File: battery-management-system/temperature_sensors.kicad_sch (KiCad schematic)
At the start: 4 parts, among them J15 TEMP_CELL1, J16 TEMP_CELL2, J17 TEMP_CELL3, J18 TEMP_CELL4

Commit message: improve layout
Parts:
- renumbered J15 to J22, J16 to J23, J17 to J24, J18 to J25
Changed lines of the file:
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@@
   (symbol (lib_id "benediktibk:rspro_header_4pin_3_5mm") (at 58.42 53.34 0) (unit 1)
     (in_bom yes) (on_board yes) (dnp no)
-    (property "Reference" "J17" (at 60.96 53.34 0)
+    (property "Reference" "J24" (at 60.96 53.34 0)
       (effects (font (size 1.27 1.27)) (justify left))
     )
@@
       (project "battery-management-system"
         (path "/5272f0ff-3069-41a9-bca2-80beede8b4b2/3cb0d78b-1dc8-4b57-8c9a-18900dc8da61"
-          (reference "J17") (unit 1)
+          (reference "J24") (unit 1)
         )
       )
@@
   (symbol (lib_id "benediktibk:rspro_header_4pin_3_5mm") (at 58.42 27.94 0) (unit 1)
     (in_bom yes) (on_board yes) (dnp no)
-    (property "Reference" "J15" (at 60.96 27.94 0)
+    (property "Reference" "J22" (at 60.96 27.94 0)
       (effects (font (size 1.27 1.27)) (justify left))
     )
@@
       (project "battery-management-system"
         (path "/5272f0ff-3069-41a9-bca2-80beede8b4b2/3cb0d78b-1dc8-4b57-8c9a-18900dc8da61"
-          (reference "J15") (unit 1)
+          (reference "J22") (unit 1)
         )
       )
@@
   (symbol (lib_id "benediktibk:rspro_header_4pin_3_5mm") (at 58.42 40.64 0) (unit 1)
     (in_bom yes) (on_board yes) (dnp no)
-    (property "Reference" "J16" (at 60.96 40.64 0)
+    (property "Reference" "J23" (at 60.96 40.64 0)
       (effects (font (size 1.27 1.27)) (justify left))
     )
@@
       (project "battery-management-system"
         (path "/5272f0ff-3069-41a9-bca2-80beede8b4b2/3cb0d78b-1dc8-4b57-8c9a-18900dc8da61"
-          (reference "J16") (unit 1)
+          (reference "J23") (unit 1)
         )
       )
@@
   (symbol (lib_id "power:GND") (at 49.53 74.93 0) (unit 1)
     (in_bom yes) (on_board yes) (dnp no) (fields_autoplaced)
-    (property "Reference" "#PWR09" (at 49.53 81.28 0)
+    (property "Reference" "#PWR082" (at 49.53 81.28 0)
       (effects (font (size 1.27 1.27)) hide)
     )
@@
       (project "battery-management-system"
         (path "/5272f0ff-3069-41a9-bca2-80beede8b4b2/3cb0d78b-1dc8-4b57-8c9a-18900dc8da61"
-          (reference "#PWR09") (unit 1)
+          (reference "#PWR082") (unit 1)
         )
       )
@@
   (symbol (lib_id "benediktibk:rspro_header_4pin_3_5mm") (at 58.42 66.04 0) (unit 1)
     (in_bom yes) (on_board yes) (dnp no)
-    (property "Reference" "J18" (at 60.96 66.04 0)
+    (property "Reference" "J25" (at 60.96 66.04 0)
       (effects (font (size 1.27 1.27)) (justify left))
     )
@@
       (project "battery-management-system"
         (path "/5272f0ff-3069-41a9-bca2-80beede8b4b2/3cb0d78b-1dc8-4b57-8c9a-18900dc8da61"
-          (reference "J18") (unit 1)
+          (reference "J25") (unit 1)
         )
       )

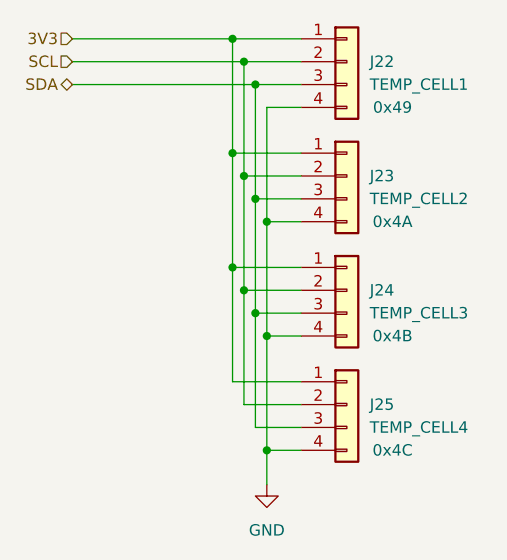
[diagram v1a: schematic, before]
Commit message: add enable input for cell measurement
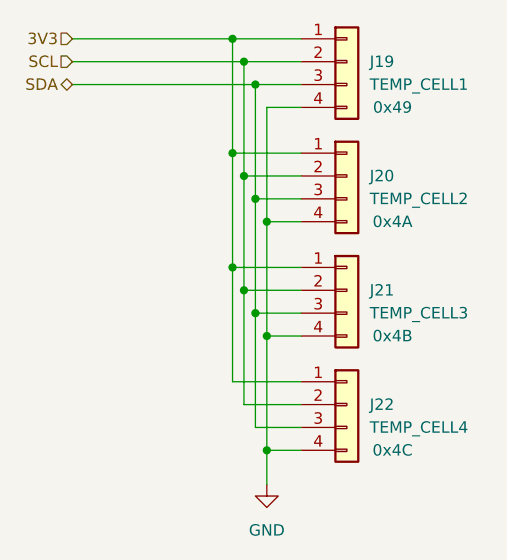
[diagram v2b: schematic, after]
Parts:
- renumbered J22 to J19, J23 to J20, J24 to J21, J25 to J22
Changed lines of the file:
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@@
   (symbol (lib_id "benediktibk:rspro_header_4pin_3_5mm") (at 58.42 53.34 0) (unit 1)
     (in_bom yes) (on_board yes) (dnp no)
-    (property "Reference" "J24" (at 60.96 53.34 0)
+    (property "Reference" "J21" (at 60.96 53.34 0)
       (effects (font (size 1.27 1.27)) (justify left))
     )
@@
       (project "battery-management-system"
         (path "/5272f0ff-3069-41a9-bca2-80beede8b4b2/3cb0d78b-1dc8-4b57-8c9a-18900dc8da61"
-          (reference "J24") (unit 1)
+          (reference "J21") (unit 1)
         )
       )
@@
   (symbol (lib_id "benediktibk:rspro_header_4pin_3_5mm") (at 58.42 27.94 0) (unit 1)
     (in_bom yes) (on_board yes) (dnp no)
-    (property "Reference" "J22" (at 60.96 27.94 0)
+    (property "Reference" "J19" (at 60.96 27.94 0)
       (effects (font (size 1.27 1.27)) (justify left))
     )
@@
       (project "battery-management-system"
         (path "/5272f0ff-3069-41a9-bca2-80beede8b4b2/3cb0d78b-1dc8-4b57-8c9a-18900dc8da61"
-          (reference "J22") (unit 1)
+          (reference "J19") (unit 1)
         )
       )
@@
   (symbol (lib_id "benediktibk:rspro_header_4pin_3_5mm") (at 58.42 40.64 0) (unit 1)
     (in_bom yes) (on_board yes) (dnp no)
-    (property "Reference" "J23" (at 60.96 40.64 0)
+    (property "Reference" "J20" (at 60.96 40.64 0)
       (effects (font (size 1.27 1.27)) (justify left))
     )
@@
       (project "battery-management-system"
         (path "/5272f0ff-3069-41a9-bca2-80beede8b4b2/3cb0d78b-1dc8-4b57-8c9a-18900dc8da61"
-          (reference "J23") (unit 1)
+          (reference "J20") (unit 1)
         )
       )
@@
   (symbol (lib_id "power:GND") (at 49.53 74.93 0) (unit 1)
     (in_bom yes) (on_board yes) (dnp no) (fields_autoplaced)
-    (property "Reference" "#PWR082" (at 49.53 81.28 0)
+    (property "Reference" "#PWR071" (at 49.53 81.28 0)
       (effects (font (size 1.27 1.27)) hide)
     )
@@
       (project "battery-management-system"
         (path "/5272f0ff-3069-41a9-bca2-80beede8b4b2/3cb0d78b-1dc8-4b57-8c9a-18900dc8da61"
-          (reference "#PWR082") (unit 1)
+          (reference "#PWR071") (unit 1)
         )
       )
@@
   (symbol (lib_id "benediktibk:rspro_header_4pin_3_5mm") (at 58.42 66.04 0) (unit 1)
     (in_bom yes) (on_board yes) (dnp no)
-    (property "Reference" "J25" (at 60.96 66.04 0)
+    (property "Reference" "J22" (at 60.96 66.04 0)
       (effects (font (size 1.27 1.27)) (justify left))
     )
@@
       (project "battery-management-system"
         (path "/5272f0ff-3069-41a9-bca2-80beede8b4b2/3cb0d78b-1dc8-4b57-8c9a-18900dc8da61"
-          (reference "J25") (unit 1)
+          (reference "J22") (unit 1)
         )
       )
